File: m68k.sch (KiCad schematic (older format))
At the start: 1 part

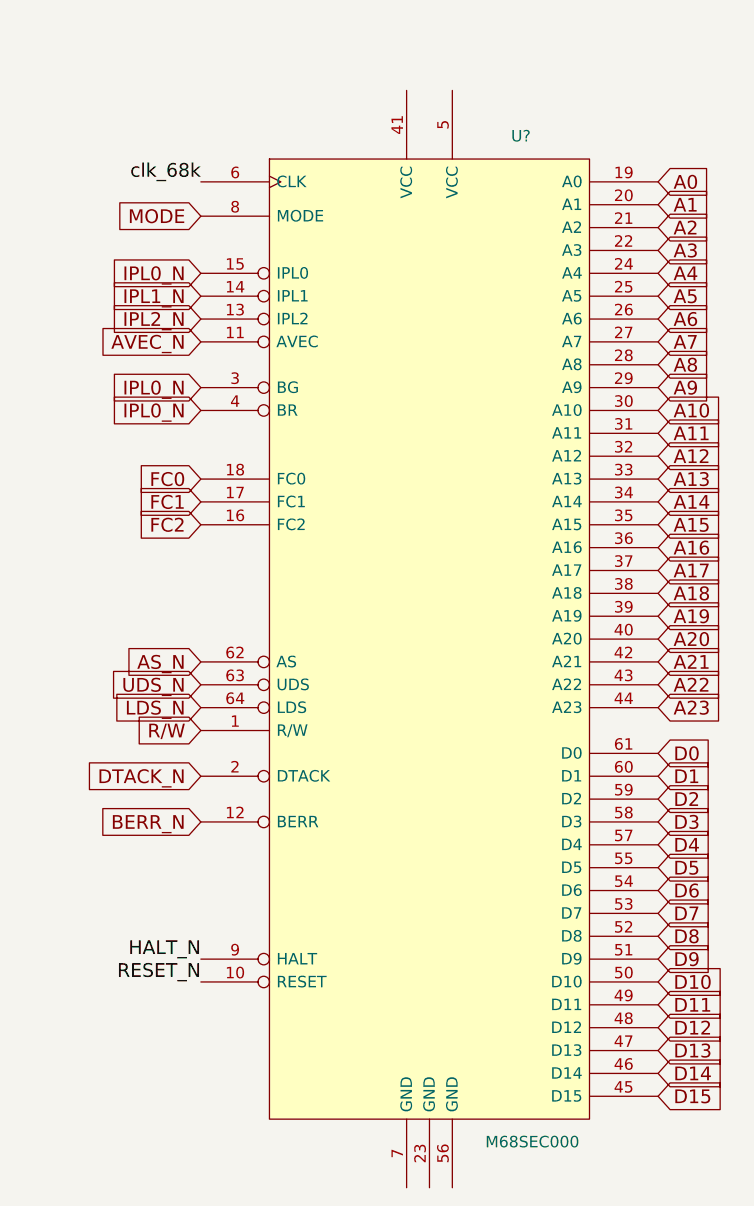
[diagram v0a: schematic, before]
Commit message: moved cpu to own sheet
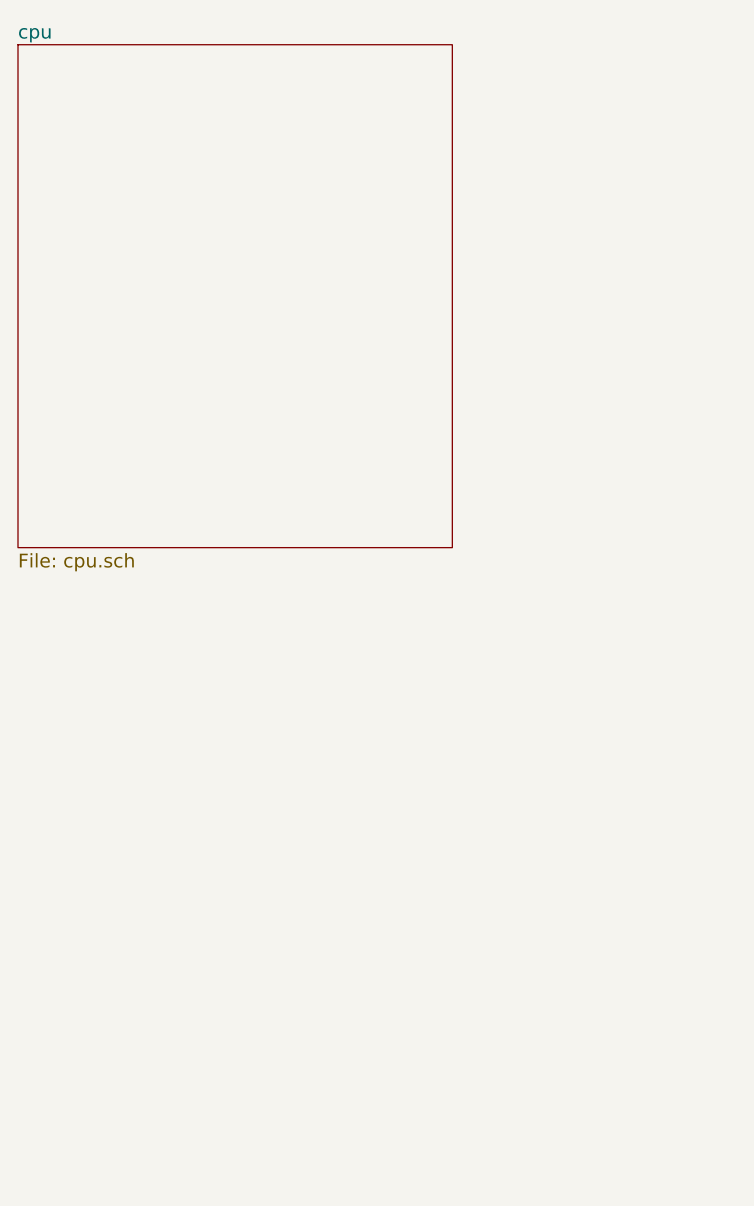
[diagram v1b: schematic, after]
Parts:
- removed U?: M68SEC000, symbol M68SEC000
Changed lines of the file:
@@
 LIBS:valves
 LIBS:custom
+LIBS:m68k-cache
 EELAYER 25 0
 EELAYER END
 $Descr A4 11693 8268
 encoding utf-8
-Sheet 1 1
+Sheet 1 2
 Title "M68k Computer"
 Date "2017-08-04"
@@
 Comment4 ""
 $EndDescr
-$Comp
-L M68SEC000 U?
-U 1 1 59845163
-P 2950 3800
-F 0 "U?" H 3350 6200 50  0000 C CNN
-F 1 "M68SEC000" H 3400 1800 50  0000 C CNN
-F 2 "" H 2950 3800 50  0001 C CNN
-F 3 "" H 2950 3800 50  0001 C CNN
-	1    2950 3800
-	1    0    0    -1
-$EndComp
-Text GLabel 3950 1600 2    60   Input ~ 0
-A0
-Text GLabel 3950 1700 2    60   Input ~ 0
-A1
-Text GLabel 3950 1800 2    60   Input ~ 0
-A2
-Text GLabel 3950 1900 2    60   Input ~ 0
-A3
-Text GLabel 3950 2000 2    60   Input ~ 0
-A4
-Text GLabel 3950 2100 2    60   Input ~ 0
-A5
-Text GLabel 3950 2200 2    60   Input ~ 0
-A6
-Text GLabel 3950 2300 2    60   Input ~ 0
-A7
-Text GLabel 3950 2400 2    60   Input ~ 0
-A8
-Text GLabel 3950 2500 2    60   Input ~ 0
-A9
-Text GLabel 3950 2600 2    60   Input ~ 0
-A10
-Text GLabel 3950 2700 2    60   Input ~ 0
-A11
-Text GLabel 3950 2800 2    60   Input ~ 0
-A12
-Text GLabel 3950 2900 2    60   Input ~ 0
-A13
-Text GLabel 3950 3000 2    60   Input ~ 0
-A14
-Text GLabel 3950 3100 2    60   Input ~ 0
-A15
-Text GLabel 3950 3200 2    60   Input ~ 0
-A16
-Text GLabel 3950 3300 2    60   Input ~ 0
-A17
-Text GLabel 3950 3400 2    60   Input ~ 0
-A18
-Text GLabel 3950 3500 2    60   Input ~ 0
-A19
-Text GLabel 3950 3600 2    60   Input ~ 0
-A20
-Text GLabel 3950 3700 2    60   Input ~ 0
-A21
-Text GLabel 3950 3800 2    60   Input ~ 0
-A22
-Text GLabel 3950 3900 2    60   Input ~ 0
-A23
-Text GLabel 3950 4100 2    60   Input ~ 0
-D0
-Text GLabel 3950 4200 2    60   Input ~ 0
-D1
-Text GLabel 3950 4300 2    60   Input ~ 0
-D2
-Text GLabel 3950 4400 2    60   Input ~ 0
-D3
-Text GLabel 3950 4500 2    60   Input ~ 0
-D4
-Text GLabel 3950 4600 2    60   Input ~ 0
-D5
-Text GLabel 3950 4700 2    60   Input ~ 0
-D6
-Text GLabel 3950 4800 2    60   Input ~ 0
-D7
-Text GLabel 3950 4900 2    60   Input ~ 0
-D8
-Text GLabel 3950 5000 2    60   Input ~ 0
-D9
-Text GLabel 3950 5100 2    60   Input ~ 0
-D10
-Text GLabel 3950 5200 2    60   Input ~ 0
-D11
-Text GLabel 3950 5300 2    60   Input ~ 0
-D12
-Text GLabel 3950 5400 2    60   Input ~ 0
-D13
-Text GLabel 3950 5500 2    60   Input ~ 0
-D14
-Text GLabel 3950 5600 2    60   Input ~ 0
-D15
-Text Label 1950 1600 2    60   ~ 0
-clk_68k
-Text GLabel 1950 1750 0    60   Input ~ 0
-MODE
-Text GLabel 1950 2000 0    60   Input ~ 0
-IPL0_N
-Text GLabel 1950 2100 0    60   Input ~ 0
-IPL1_N
-Text GLabel 1950 2200 0    60   Input ~ 0
-IPL2_N
-Text GLabel 1950 2300 0    60   Input ~ 0
-AVEC_N
-Text GLabel 1950 2500 0    60   Input ~ 0
-IPL0_N
-Text GLabel 1950 2600 0    60   Input ~ 0
-IPL0_N
-Text GLabel 1950 2900 0    60   Input ~ 0
-FC0
-Text GLabel 1950 3000 0    60   Input ~ 0
-FC1
-Text GLabel 1950 3100 0    60   Input ~ 0
-FC2
-Text GLabel 1950 3700 0    60   Input ~ 0
-AS_N
-Text GLabel 1950 3800 0    60   Input ~ 0
-UDS_N
-Text GLabel 1950 3900 0    60   Input ~ 0
-LDS_N
-Text GLabel 1950 4000 0    60   Input ~ 0
-R/W
-Text GLabel 1950 4200 0    60   Input ~ 0
-DTACK_N
-Text GLabel 1950 4400 0    60   Input ~ 0
-BERR_N
-Text Label 1950 5000 2    60   ~ 0
-HALT_N
-Text Label 1950 5100 2    60   ~ 0
-RESET_N
+$Sheet
+S 1150 1000 1900 2200
+U 59846BBA
+F0 "cpu" 60
+F1 "cpu.sch" 60
+$EndSheet
 $EndSCHEMATC

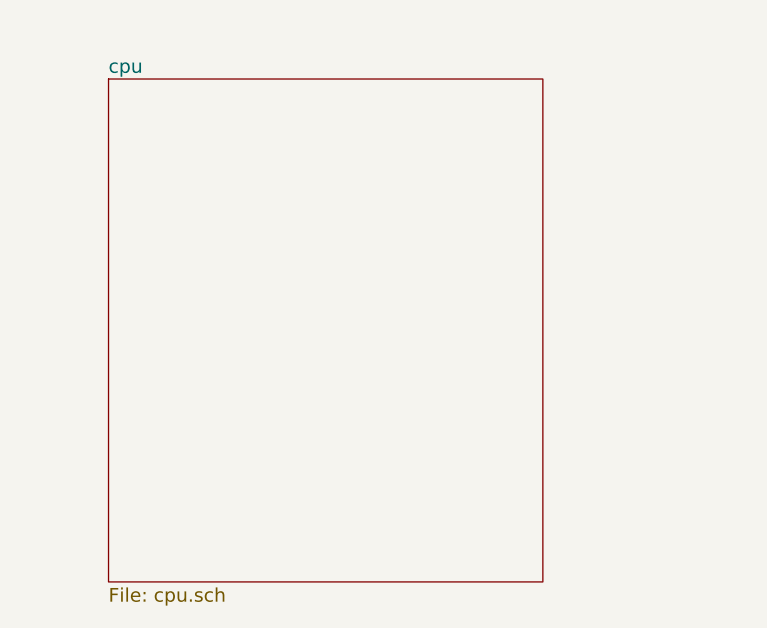
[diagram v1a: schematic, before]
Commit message: added sram symbol
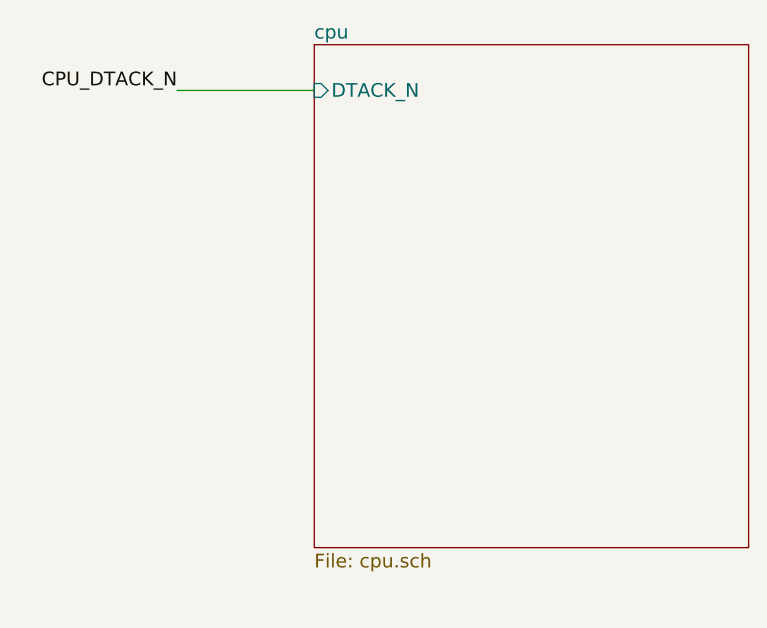
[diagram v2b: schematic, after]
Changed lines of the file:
@@
 $EndDescr
 $Sheet
-S 1150 1000 1900 2200
+S 2050 850  1900 2200
 U 59846BBA
 F0 "cpu" 60
 F1 "cpu.sch" 60
+F2 "DTACK_N" I L 2050 1050 60
 $EndSheet
+Wire Wire Line
+	2050 1050 1450 1050
+Text Label 1450 1050 2    60   ~ 0
+CPU_DTACK_N
 $EndSCHEMATC

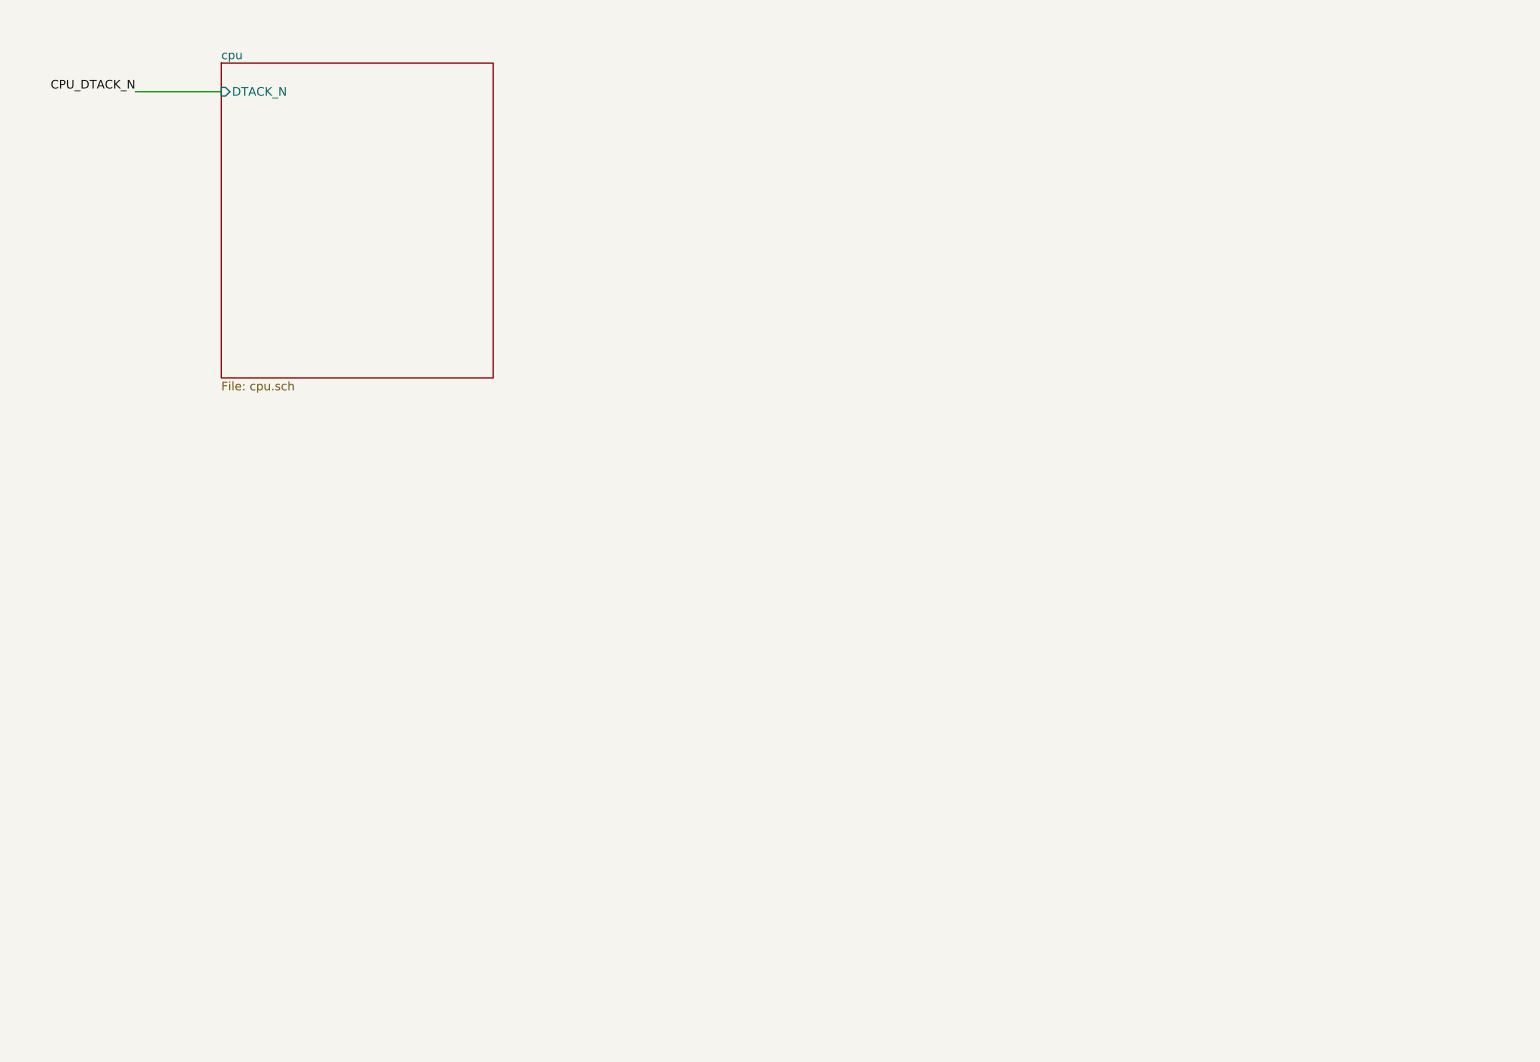
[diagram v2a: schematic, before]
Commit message: moved all components onto top sheet
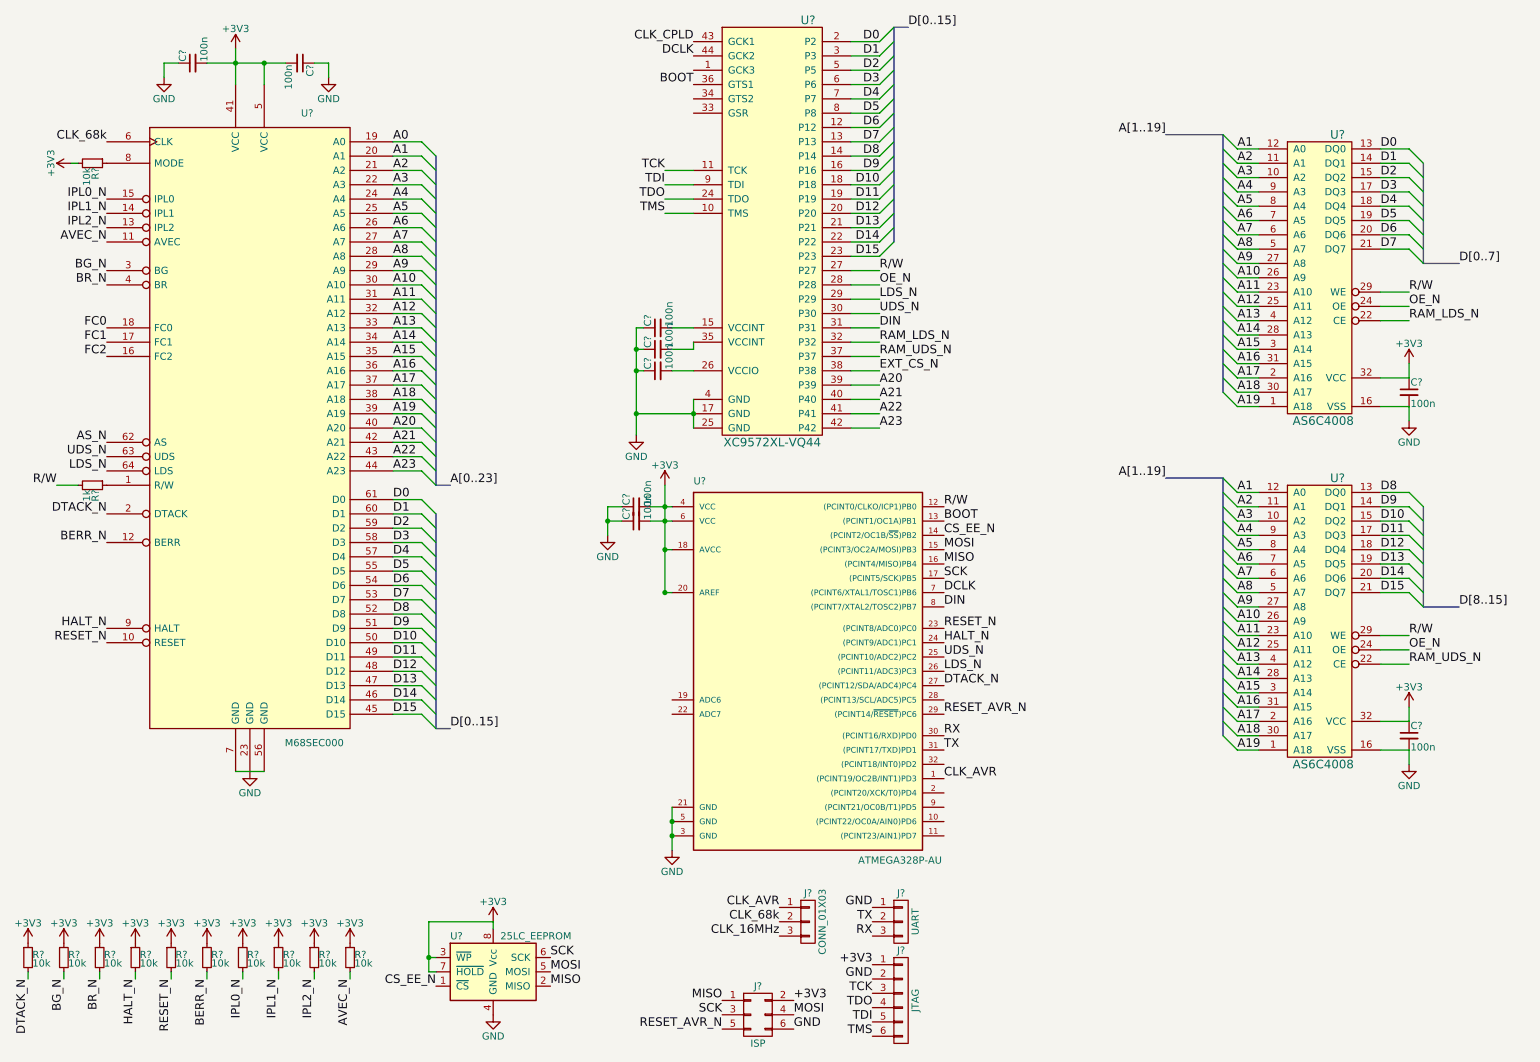
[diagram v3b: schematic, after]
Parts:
- added C? (x9): 100n, symbol C_Small
- added J?: ISP, symbol CONN_02X03
- added J?: JTAG, symbol CONN_01X06
- added J?: UART, symbol CONN_01X03
- added J?: CONN_01X03, symbol CONN_01X03
- added R? (x11): 10k, symbol R_Small
- added R?: 1k, symbol R_Small
- added U?: M68SEC000, symbol M68SEC000
- added U?: 25LC_EEPROM, symbol 25LC_EEPROM
- added U? (x2): AS6C4008, symbol AS6C4008
- added U?: XC9572XL-VQ44, symbol XC9572XL-VQ44
- added U?: ATMEGA328P-AU, TQFP32, symbol ATMEGA328P-AU
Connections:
- new net: R?.1, U?.1 (R/W)
- new net: U?.56 (GND), U?.7 (GND)
- new net: R?.1, U?.8 (MODE)
- new net: C?.2, U?.15 (VCCINT)
- new net: C?.2, U?.26 (VCCIO)
- new net: C?.2, U?.35 (VCCINT)
- new net +3V3: C?.1, C?.1, C?.2, C?.2, C?.2, C?.2, J?.1 (P1), J?.2 (P2), R?.1, R?.1, R?.1, R?.1, R?.1, R?.1, R?.1, R?.1, R?.1, R?.1, R?.2, U?.18 (AVCC), U?.20 (AREF), U?.3 (~WP), U?.32 (VCC), U?.32 (VCC), U?.4 (VCC), U?.41 (VCC), U?.5 (VCC), U?.6 (VCC), U?.7 (~HOLD), U?.8 (Vcc)
- new net A0: U?.19 (A0)
- new net A1: U?.12 (A0), U?.12 (A0), U?.20 (A1)
- new net A10: U?.26 (A9), U?.26 (A9), U?.30 (A10)
- new net A11: U?.23 (A10), U?.23 (A10), U?.31 (A11)
- new net A12: U?.25 (A11), U?.25 (A11), U?.32 (A12)
- new net A13: U?.33 (A13), U?.4 (A12), U?.4 (A12)
- new net A14: U?.28 (A13), U?.28 (A13), U?.34 (A14)
- new net A15: U?.3 (A14), U?.3 (A14), U?.35 (A15)
- new net A16: U?.31 (A15), U?.31 (A15), U?.36 (A16)
- new net A17: U?.2 (A16), U?.2 (A16), U?.37 (A17)
- new net A18: U?.30 (A17), U?.30 (A17), U?.38 (A18)
- new net A19: U?.1 (A18), U?.1 (A18), U?.39 (A19)
- new net A2: U?.11 (A1), U?.11 (A1), U?.21 (A2)
- new net A20: U?.39 (P39), U?.40 (A20)
- new net A21: U?.40 (P40), U?.42 (A21)
- new net A22: U?.41 (P41), U?.43 (A22)
- new net A23: U?.42 (P42), U?.44 (A23)
- new net A3: U?.10 (A2), U?.10 (A2), U?.22 (A3)
- new net A4: U?.24 (A4), U?.9 (A3), U?.9 (A3)
- new net A5: U?.25 (A5), U?.8 (A4), U?.8 (A4)
- new net A6: U?.26 (A6), U?.7 (A5), U?.7 (A5)
- new net A7: U?.27 (A7), U?.6 (A6), U?.6 (A6)
- new net A8: U?.28 (A8), U?.5 (A7), U?.5 (A7)
- new net A9: U?.27 (A8), U?.27 (A8), U?.29 (A9)
- new net AS_N: U?.62 (AS)
- new net AVEC_N: R?.2, U?.11 (AVEC)
- new net BERR_N: R?.2, U?.12 (BERR)
- new net BG_N: R?.2, U?.3 (BG)
- new net BOOT: U?.13 ((PCINT1/OC1A)PB1), U?.36 (GTS1)
- new net BR_N: R?.2, U?.4 (BR)
- new net CLK_16MHz: J?.3 (P3)
- new net CLK_68k: J?.2 (P2), U?.6 (CLK)
- new net CLK_AVR: J?.1 (P1), U?.1 ((PCINT19/OC2B/INT1)PD3)
- new net CLK_CPLD: U?.43 (GCK1)
- new net CS_EE_N: U?.1 (~CS), U?.14 ((PCINT2/OC1B/~SS~)PB2)
- new net D0: U?.13 (DQ0), U?.2 (P2), U?.61 (D0)
- new net D1: U?.14 (DQ1), U?.3 (P3), U?.60 (D1)
- new net D10: U?.15 (DQ2), U?.18 (P18), U?.50 (D10)
- new net D11: U?.17 (DQ3), U?.19 (P19), U?.49 (D11)
- new net D12: U?.18 (DQ4), U?.20 (P20), U?.48 (D12)
- new net D13: U?.19 (DQ5), U?.21 (P21), U?.47 (D13)
- new net D14: U?.20 (DQ6), U?.22 (P22), U?.46 (D14)
- new net D15: U?.21 (DQ7), U?.23 (P23), U?.45 (D15)
- new net D2: U?.15 (DQ2), U?.5 (P5), U?.59 (D2)
- new net D3: U?.17 (DQ3), U?.58 (D3), U?.6 (P6)
- new net D4: U?.18 (DQ4), U?.57 (D4), U?.7 (P7)
- new net D5: U?.19 (DQ5), U?.55 (D5), U?.8 (P8)
- new net D6: U?.12 (P12), U?.20 (DQ6), U?.54 (D6)
- new net D7: U?.13 (P13), U?.21 (DQ7), U?.53 (D7)
- new net D8: U?.13 (DQ0), U?.14 (P14), U?.52 (D8)
- new net D9: U?.14 (DQ1), U?.16 (P16), U?.51 (D9)
- new net DCLK: U?.44 (GCK2), U?.7 ((PCINT6/XTAL1/TOSC1)PB6)
- new net DIN: U?.31 (P31), U?.8 ((PCINT7/XTAL2/TOSC2)PB7)
- new net DTACK_N: R?.2, U?.2 (DTACK), U?.27 ((PCINT12/SDA/ADC4)PC4)
- new net EXT_CS_N: U?.38 (P38)
- new net FC0: U?.18 (FC0)
- new net FC1: U?.17 (FC1)
- new net FC2: U?.16 (FC2)
- new net GND: C?.1, C?.1, C?.1, C?.1, C?.1, C?.1, C?.1, C?.2, C?.2, J?.1 (P1), J?.2 (P2), J?.6 (P6), U?.16 (VSS), U?.16 (VSS), U?.17 (GND), U?.21 (GND), U?.23 (GND), U?.25 (GND), U?.3 (GND), U?.4 (GND), U?.4 (GND), U?.5 (GND)
- new net HALT_N: R?.2, U?.24 ((PCINT9/ADC1)PC1), U?.9 (HALT)
- new net IPL0_N: R?.2, U?.15 (IPL0)
- new net IPL1_N: R?.2, U?.14 (IPL1)
- new net IPL2_N: R?.2, U?.13 (IPL2)
- new net LDS_N: U?.26 ((PCINT11/ADC3)PC3), U?.29 (P29), U?.64 (LDS)
- new net MISO: J?.1 (P1), U?.16 ((PCINT4/MISO)PB4), U?.2 (MISO)
- new net MOSI: J?.4 (P4), U?.15 ((PCINT3/OC2A/MOSI)PB3), U?.5 (MOSI)
- new net OE_N: U?.24 (OE), U?.24 (OE), U?.28 (P28)
- new net R/W: R?.2, U?.12 ((PCINT0/CLKO/ICP1)PB0), U?.27 (P27), U?.29 (WE), U?.29 (WE)
- new net RAM_LDS_N: U?.22 (CE), U?.32 (P32)
- new net RAM_UDS_N: U?.22 (CE), U?.37 (P37)
- new net RESET_AVR_N: J?.5 (P5), U?.29 ((PCINT14/~RESET~)PC6)
- new net RESET_N: R?.2, U?.10 (RESET), U?.23 ((PCINT8/ADC0)PC0)
- new net RX: J?.3 (P3), U?.30 ((PCINT16/RXD)PD0)
- new net SCK: J?.3 (P3), U?.17 ((PCINT5/SCK)PB5), U?.6 (SCK)
- new net TCK: J?.3 (P3), U?.11 (TCK)
- new net TDI: J?.5 (P5), U?.9 (TDI)
- new net TDO: J?.4 (P4), U?.24 (TDO)
- new net TMS: J?.6 (P6), U?.10 (TMS)
- new net TX: J?.2 (P2), U?.31 ((PCINT17/TXD)PD1)
- new net UDS_N: U?.25 ((PCINT10/ADC2)PC2), U?.30 (P30), U?.63 (UDS)

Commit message: added voltage regulator
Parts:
- added C? (x2): C_Small, symbol C_Small
- added J?: CONN_02X25, symbol CONN_02X25
- added U?: LM1117-3.3, symbol LM1117-3.3
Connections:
- net EXT_CS_N is gone; now on net BERR_N: U?.38 (P38)
- net +3V3: now also C?.1, U?.2 (VO), U?.4 (VO)
- net DTACK_N: now also U?.34 (GTS2)
- net GND: now also C?.2, C?.2, U?.1 (GND/ADJ)
- new net +5V: C?.1, U?.3 (VI)
